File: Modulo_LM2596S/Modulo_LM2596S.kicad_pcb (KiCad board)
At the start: 2 copper layers, 48.8 x 26.6 mm, 21 parts, among them J101 Conn_01x01_Female, J102 Conn_01x01_Female, J103 Conn_01x01_Female, J104 Conn_01x01_Female, J105 Conn_01x01_Female, J106 Conn_01x01_Female, J107 Conn_01x01_Female, J108 Conn_01x01_Female, U101 LM2596S-ADJ

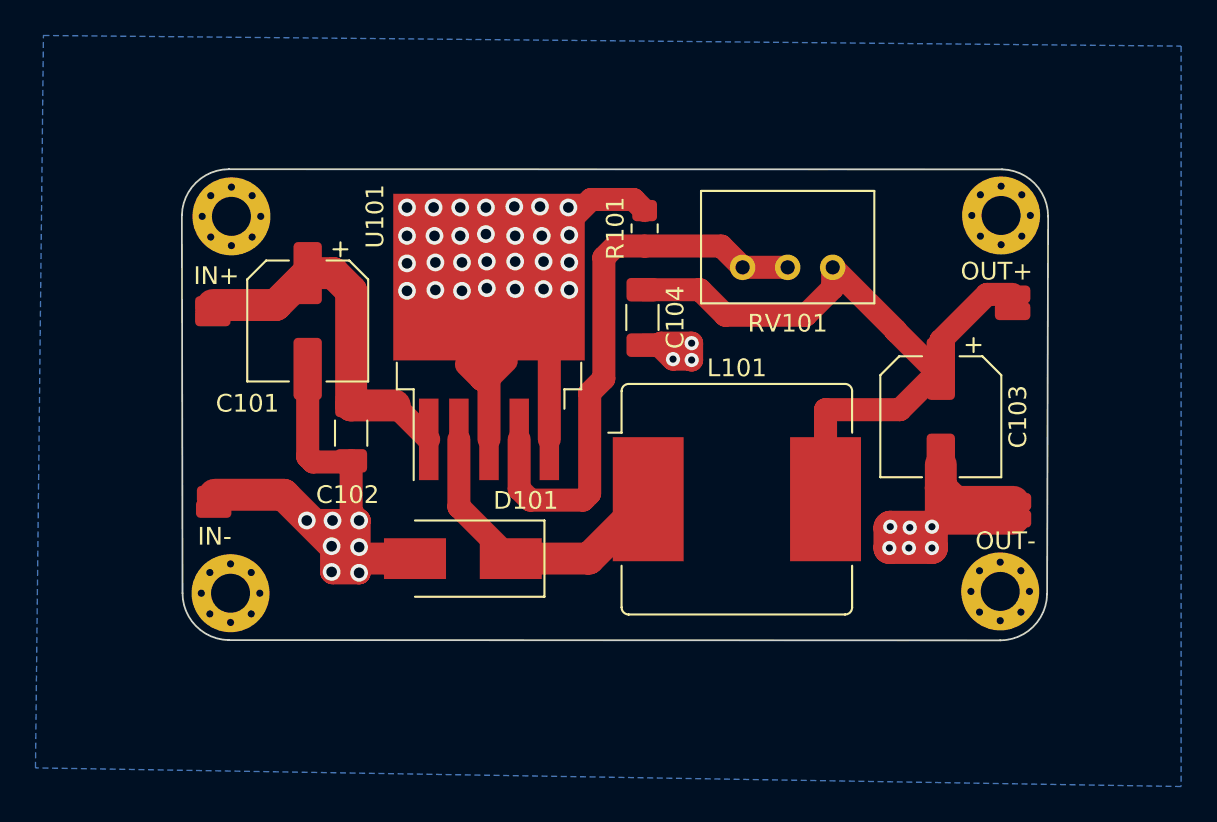
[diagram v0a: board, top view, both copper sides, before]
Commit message: LM2596S: Test di fillzone
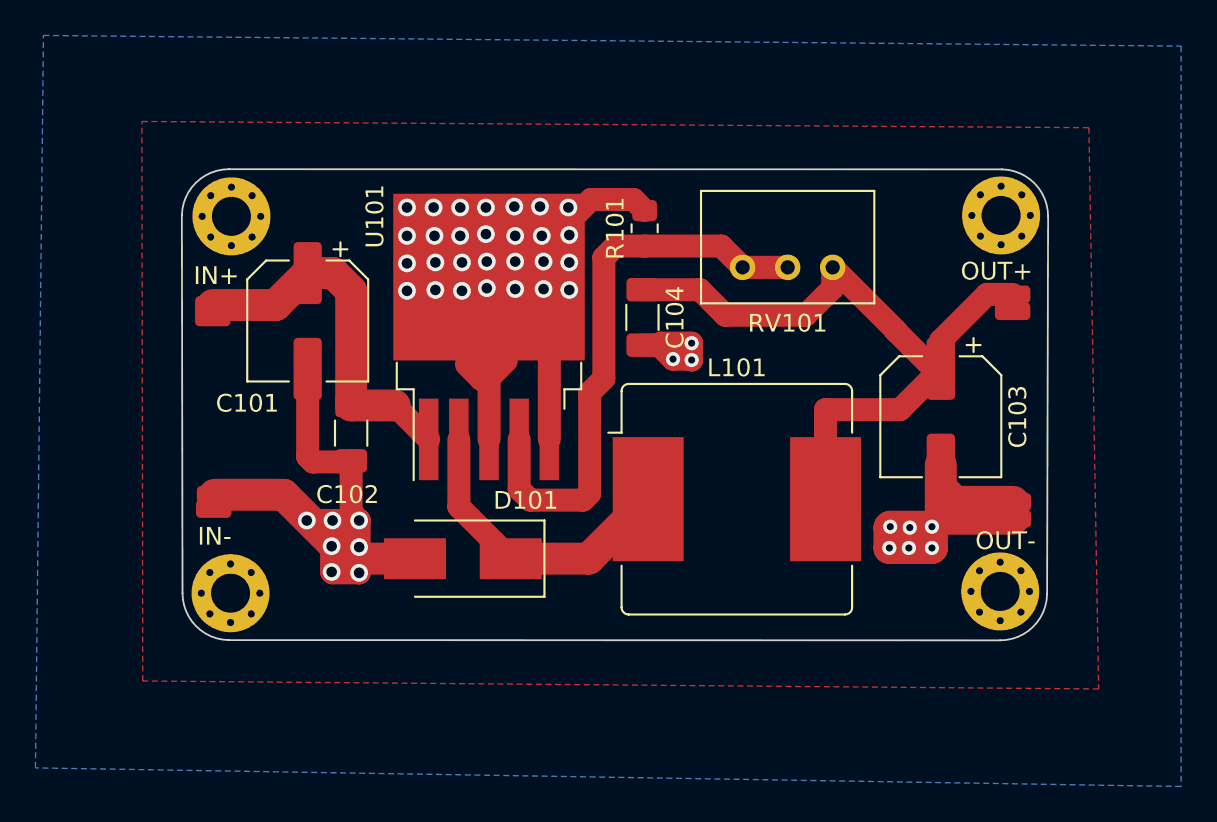
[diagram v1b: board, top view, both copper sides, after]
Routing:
- added copper zone on F.Cu, net OUT-
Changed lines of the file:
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@@
   (segment (start 174.75 90.45) (end 178.1 87.1) (width 1.8) (layer "F.Cu") (net 5))
   (segment (start 167.425 87.525) (end 170.35 90.45) (width 1.3) (layer "F.Cu") (net 5))
+  (zone (net 3) (net_name "OUT-") (layer "F.Cu") (hatch edge 0.508)
+    (connect_pads (clearance 0.508))
+    (min_thickness 0.254)
+    (fill (thermal_gap 0.508) (thermal_bridge_width 0.508))
+    (polygon
+      (pts
+        (xy 202.95 66.15)
+        (xy 203.5 97.8)
+        (xy 149.6 97.35)
+        (xy 149.55 65.8)
+      )
+    )
+  )
   (zone (net 3) (net_name "OUT-") (layer "B.Cu") (hatch edge 0.508)
     (connect_pads (clearance 0.508))
